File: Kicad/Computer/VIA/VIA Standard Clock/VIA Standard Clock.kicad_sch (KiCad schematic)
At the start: 13 parts, among them IC2 74LVC4245APW,118, IC2 AP7365-33WG-7, IC3 74LVC2G74DP,125, IC5 74LVC244APW,118, IC8 74LVC257APW,118, J1 Conn_02x16_Counter_Clockwise

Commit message: Silkscreening for VIA VIA Standard Clock.
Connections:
- net ~{Reset}_{OUT}: now also J1.15 (Pin_15)
- no-connect marks 17 -> 16
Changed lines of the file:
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@@
   )
   (no_connect (at -40.64 170.815))
-  (no_connect (at -27.94 168.275))
   (no_connect (at 132.08 189.865))
   (no_connect (at -27.94 155.575))
@@
     (effects (font (size 1.27 1.27)) (justify right bottom))
   )
+  (label "~{Reset}_{OUT}" (at -27.94 168.275 0) (fields_autoplaced)
+    (effects (font (size 1.27 1.27)) (justify left bottom))
+  )
   (label "H1" (at 132.08 134.62 0) (fields_autoplaced)

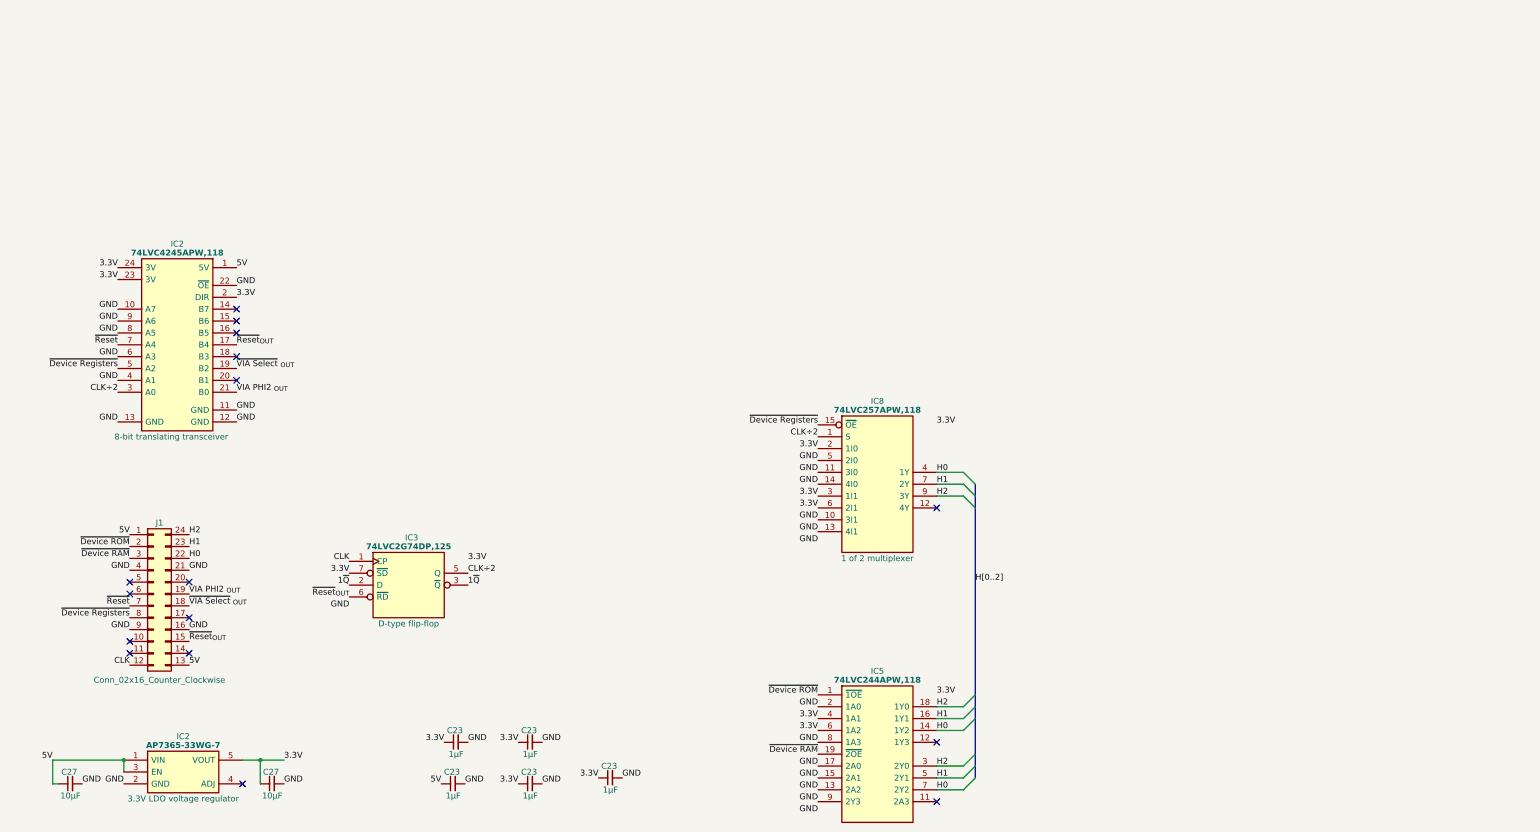
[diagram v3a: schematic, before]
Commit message: Added a VIA Control board and re-routed the VIA Board.
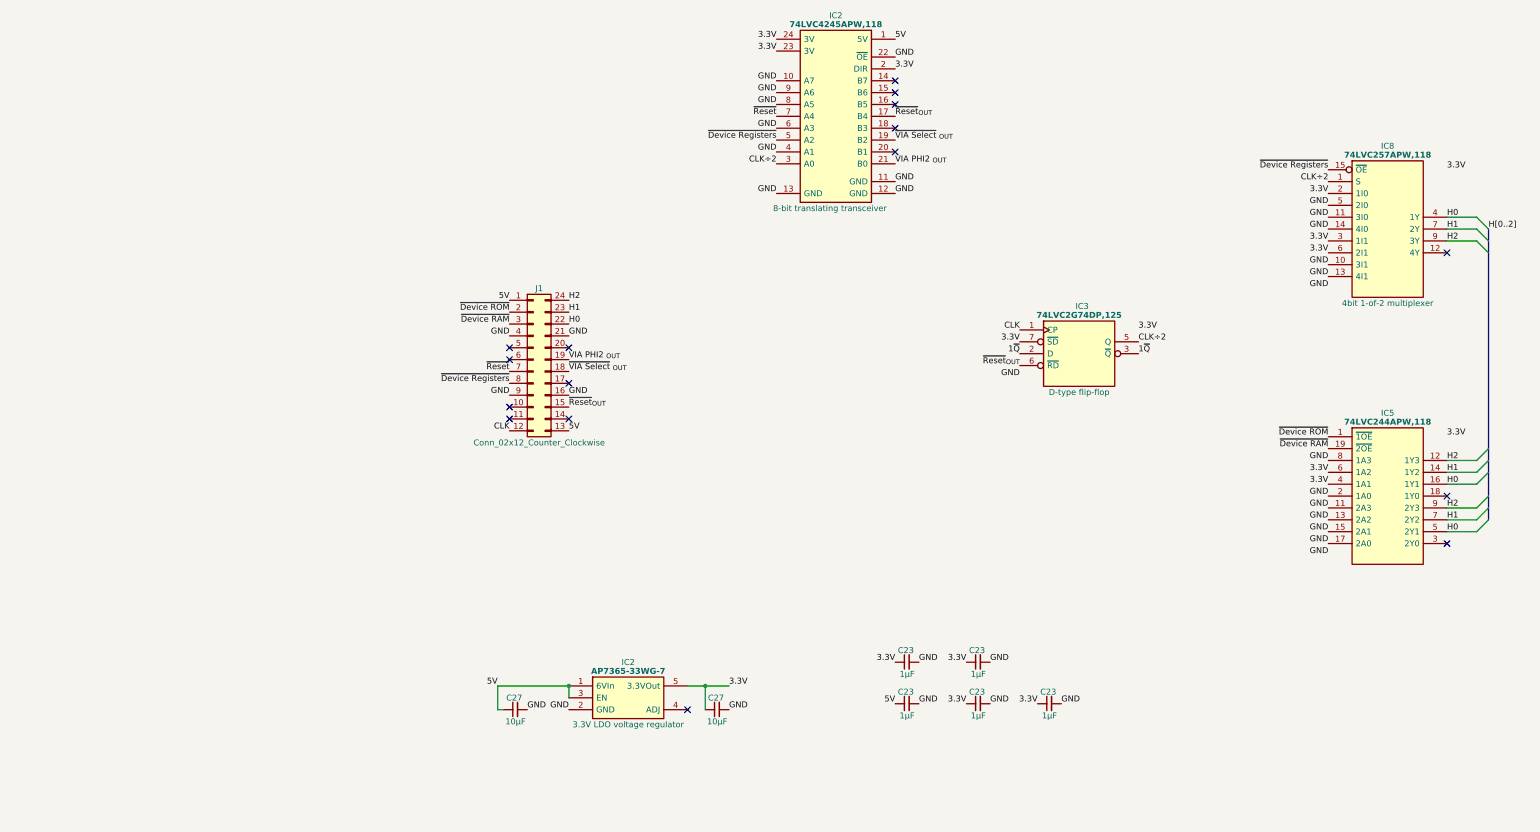
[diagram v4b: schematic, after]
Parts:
- IC2: footprint SOT95P285X130-5N -> SamacSys_Parts:SOT95P285X130-5N; Garbage (none) -> DiodesZetex AP7365-33WG-7, LDO Voltage Regulator, 600mA, 3.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
- IC2: footprint SOP65P640X110-24N -> SamacSys_Parts:SOP65P640X110-24N; Garbage (none) -> 74LVC4245A - Octal dual supply translating transceiver; 3-s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
- IC3: footprint SOP65P400X110-8N -> SamacSys_Parts:SOP65P400X110-8N; Garbage (none) -> 74LVC2G74 - Single D-type flip-flop with set and reset; pos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
- IC5: footprint SOP65P640X110-20N -> SamacSys_Parts:SOP65P640X110-20N; Garbage (none) -> 74LVC(H)244A - Octal buffer/line driver; 3-state@en-us
- IC8: footprint SOP65P640X110-16N -> SamacSys_Parts:SOP65P640X110-16N; Garbage (none) -> NEXPERIA - 74LVC157APW,118 - MUX, QUAD, 8 I/P, TSSOP-16
- J1: value Conn_02x16_Counter_Clockwise -> Conn_02x12_Counter_Clockwise
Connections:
- net GND: now also IC5.11 (2A3); no longer IC5.9 (2Y3)
- net H0: now also IC5.16 (1Y1), IC5.5 (2Y1); no longer IC5.14 (1Y2), IC5.7 (2Y2)
- net H1: now also IC5.14 (1Y2), IC5.7 (2Y2); no longer IC5.16 (1Y1), IC5.5 (2Y1)
- net H2: now also IC5.12 (1Y3), IC5.9 (2Y3); no longer IC5.18 (1Y0), IC5.3 (2Y0)
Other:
- title: (none) -> VIA Standard Clock
- moved on the sheet: C23, C27, IC2, IC3, IC5, IC8, J1
